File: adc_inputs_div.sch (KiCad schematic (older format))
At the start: 6 parts

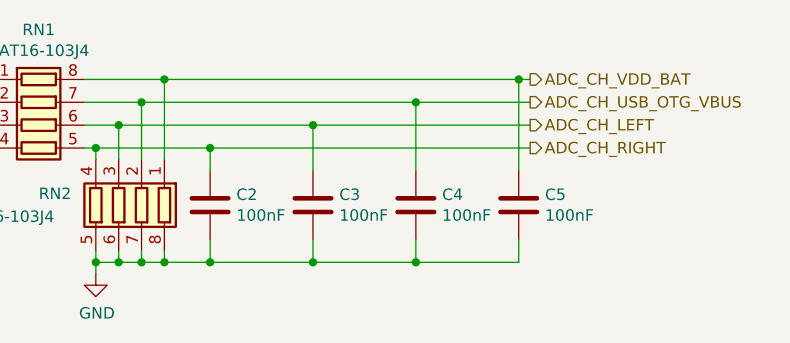
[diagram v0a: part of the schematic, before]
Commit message: Запитал МК, добавил цепи питания, тактирования, модуль клавиатуры.
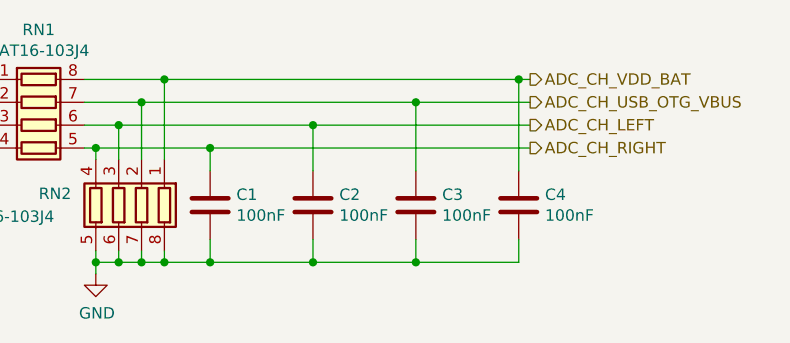
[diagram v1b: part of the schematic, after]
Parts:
- renumbered C2 to C1, C3 to C2, C4 to C3, C5 to C4
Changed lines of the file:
@@
 $Descr A4 11693 8268
 encoding utf-8
-Sheet 4 5
+Sheet 3 9
 Title ""
 Date ""
@@
 $EndDescr
 $Comp
-L Device:C C2
+L Device:C C1
 U 1 1 5E9B72C3
 P 5450 3950
-F 0 "C2" H 5565 3996 50  0000 L CNN
+F 0 "C1" H 5565 3996 50  0000 L CNN
 F 1 "100nF" H 5565 3905 50  0000 L CNN
 F 2 "Capacitor_SMD:C_0603_1608Metric_Pad1.05x0.95mm_HandSolder" H 5488 3800 50  0001 C CNN
@@
 $EndComp
 $Comp
-L Device:C C3
+L Device:C C2
 U 1 1 5E9B72ED
 P 5900 3950
-F 0 "C3" H 6015 3996 50  0000 L CNN
+F 0 "C2" H 6015 3996 50  0000 L CNN
 F 1 "100nF" H 6015 3905 50  0000 L CNN
 F 2 "Capacitor_SMD:C_0603_1608Metric_Pad1.05x0.95mm_HandSolder" H 5938 3800 50  0001 C CNN
@@
 $EndComp
 $Comp
-L Device:C C4
+L Device:C C3
 U 1 1 5E9B731A
 P 6350 3950
-F 0 "C4" H 6465 3996 50  0000 L CNN
+F 0 "C3" H 6465 3996 50  0000 L CNN
 F 1 "100nF" H 6465 3905 50  0000 L CNN
 F 2 "Capacitor_SMD:C_0603_1608Metric_Pad1.05x0.95mm_HandSolder" H 6388 3800 50  0001 C CNN
@@
 $EndComp
 $Comp
-L Device:C C5
+L Device:C C4
 U 1 1 5E9B7343
 P 6800 3950
-F 0 "C5" H 6915 3996 50  0000 L CNN
+F 0 "C4" H 6915 3996 50  0000 L CNN
 F 1 "100nF" H 6915 3905 50  0000 L CNN
 F 2 "Capacitor_SMD:C_0603_1608Metric_Pad1.05x0.95mm_HandSolder" H 6838 3800 50  0001 C CNN
@@
 	5250 3400 5250 3750
 $Comp
-L power:GND #PWR018
+L power:GND #PWR08
 U 1 1 5E9C6C4C
 P 4950 4250
-F 0 "#PWR018" H 4950 4000 50  0001 C CNN
+F 0 "#PWR08" H 4950 4000 50  0001 C CNN
 F 1 "GND" H 4955 4077 50  0000 C CNN
 F 2 "" H 4950 4250 50  0001 C CNN

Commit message: Расставил проверенные блоки в столбец.
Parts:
- added C34, C35, C36, C37, C38, C39, C40: 100nF, Capacitor_SMD:C_0603_1608Metric_Pad1.05x0.95mm_HandSolder, symbol Device:C
- added RN6, RN7, RN8, RN9: CAT16-103J4, Resistor_SMD:R_Cat16-4, symbol Device:R_Pack04
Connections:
- net GND: now also C34.2, C35.2, C36.2, C37.2, C38.2, C39.2, C40.2, RN8.5 (R4.2), RN8.6 (R3.2), RN8.7 (R2.2), RN8.8 (R1.2), RN9.5 (R4.2), RN9.6 (R3.2), RN9.7 (R2.2)
- net ADC_CH_USB_OTG_VBUS renamed ADC_CH_VDD_USB
- net USB_OTG_VBUS renamed VDD_USB
- new net A1: RN6.1 (R1.1)
- new net A2: RN6.4 (R4.1)
- new net ADC_CH_A1: C40.1, RN6.8 (R1.2), RN8.1 (R1.1)
- new net ADC_CH_A2: C34.1, RN6.5 (R4.2), RN8.4 (R4.1)
- new net ADC_CH_B1: C38.1, RN6.7 (R2.2), RN8.2 (R2.1)
- new net ADC_CH_B2: C39.1, RN7.7 (R2.2), RN9.2 (R2.1)
- new net ADC_CH_BIPPER: C35.1, RN7.5 (R4.2), RN9.4 (R4.1)
- new net ADC_CH_C1: C36.1, RN6.6 (R3.2), RN8.3 (R3.1)
- new net ADC_CH_C2: C37.1, RN7.6 (R3.2), RN9.3 (R3.1)
- new net B1: RN6.2 (R2.1)
- new net B2: RN7.2 (R2.1)
- new net C1: RN6.3 (R3.1)
- new net C2: RN7.3 (R3.1)
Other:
- moved on the sheet: C1, C2, C3, C4, RN1, RN2
